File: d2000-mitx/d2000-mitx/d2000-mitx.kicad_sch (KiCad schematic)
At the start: 47 parts, among them J1 USB 3.1 + PD INPUT, J2 87715-9306, J3 USB3_A_Stacked, J4 M.2_NVME, J5 Conn_02x10_Top_Bottom, J6 M.2_WIFI, J7 ATX-24, U1 MPQ8645PGVT-0000-Z, U10 TPS784105QWDRBRQ1, U11 TPS784105QWDRBRQ1, U12 VL805 REAR I/O, U13 RP2040, U2 MPQ8645PGVT-0000-Z, U4 FUSB302B01MPX, U6 MPQ8645PGVT-0000-Z, U7 MPQ8645PGVT-0000-Z, U8 W25Q32JVSS, U9 VL805 REAR I/O, Y1 Crystal_GND23, Y2 Crystal_GND23, Y3 12MHz

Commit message: d2000-mitx: add d2000 footprint
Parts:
- U3: footprint (none) -> D2000:D2000_DDR4_BGA1144P100_3500X350
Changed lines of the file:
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@@
 			)
 		)
-		(property "Footprint" ""
+		(property "Footprint" "D2000:D2000_DDR4_BGA1144P100_3500X350"
 			(at 473.7101 161.2899 0)
 			(effects
@@
 			)
 		)
-		(property "Footprint" ""
+		(property "Footprint" "D2000:D2000_DDR4_BGA1144P100_3500X350"
 			(at 500.3801 -50.8001 0)
 			(effects
@@
 			)
 		)
-		(property "Footprint" ""
+		(property "Footprint" "D2000:D2000_DDR4_BGA1144P100_3500X350"
 			(at 297.1801 -78.7401 0)
 			(effects
@@
 			)
 		)
-		(property "Footprint" ""
+		(property "Footprint" "D2000:D2000_DDR4_BGA1144P100_3500X350"
 			(at 481.3301 386.0799 0)
 			(effects
@@
 	)
 	(symbol
-		(lib_name "D2000:D2000-E8")
 		(lib_id "D2000:D2000-E8")
 		(at 768.35 368.3 0)
@@
 			)
 		)
-		(property "Footprint" ""
+		(property "Footprint" "D2000:D2000_DDR4_BGA1144P100_3500X350"
 			(at 834.3901 116.8399 0)
 			(effects
@@
 			)
 		)
-		(property "Footprint" ""
+		(property "Footprint" "D2000:D2000_DDR4_BGA1144P100_3500X350"
 			(at 217.1701 344.1699 0)
 			(effects

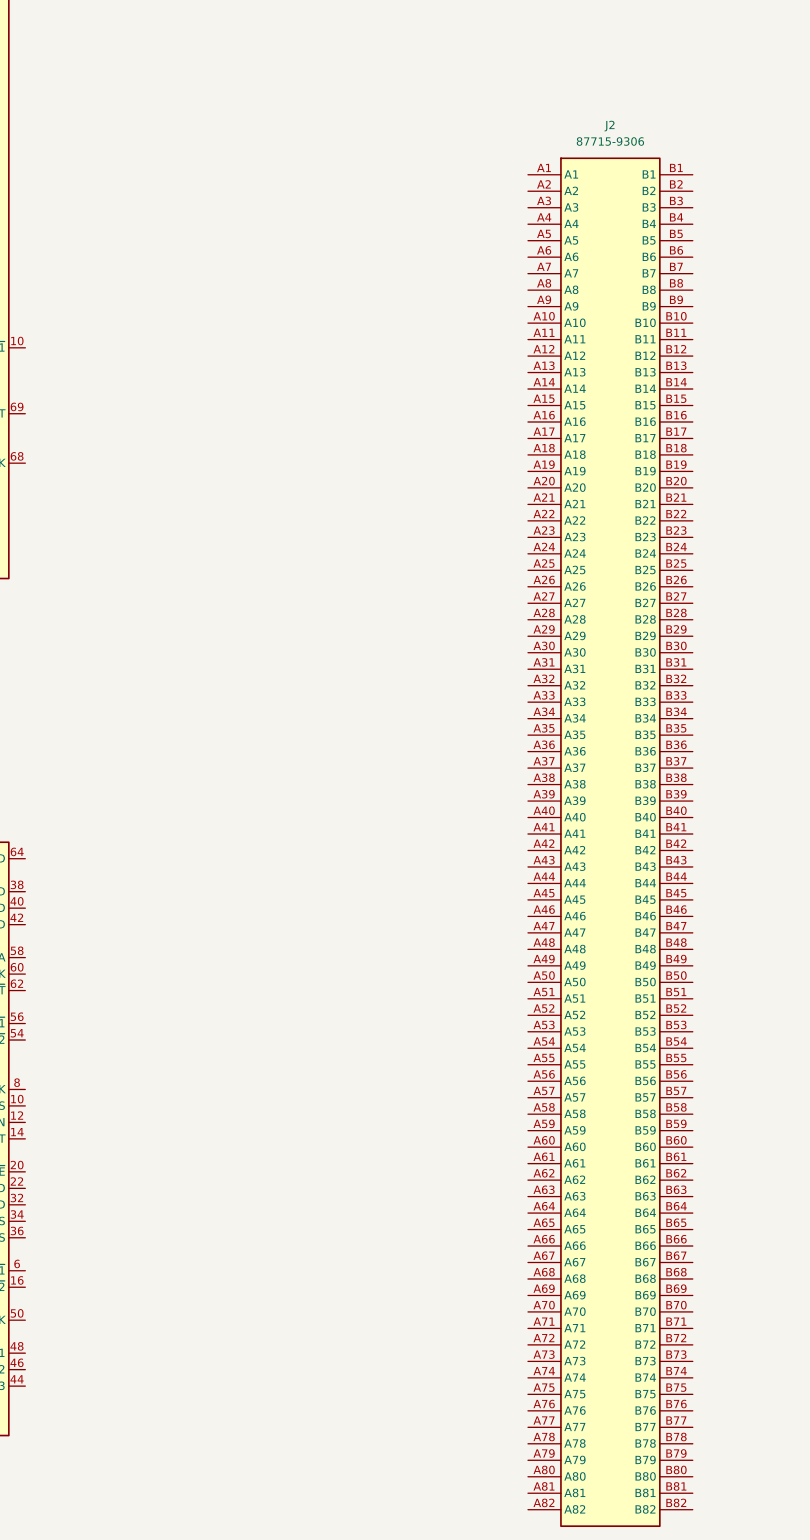
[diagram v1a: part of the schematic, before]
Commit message: d2000-mitx: slight schem tweaks, rough board placements
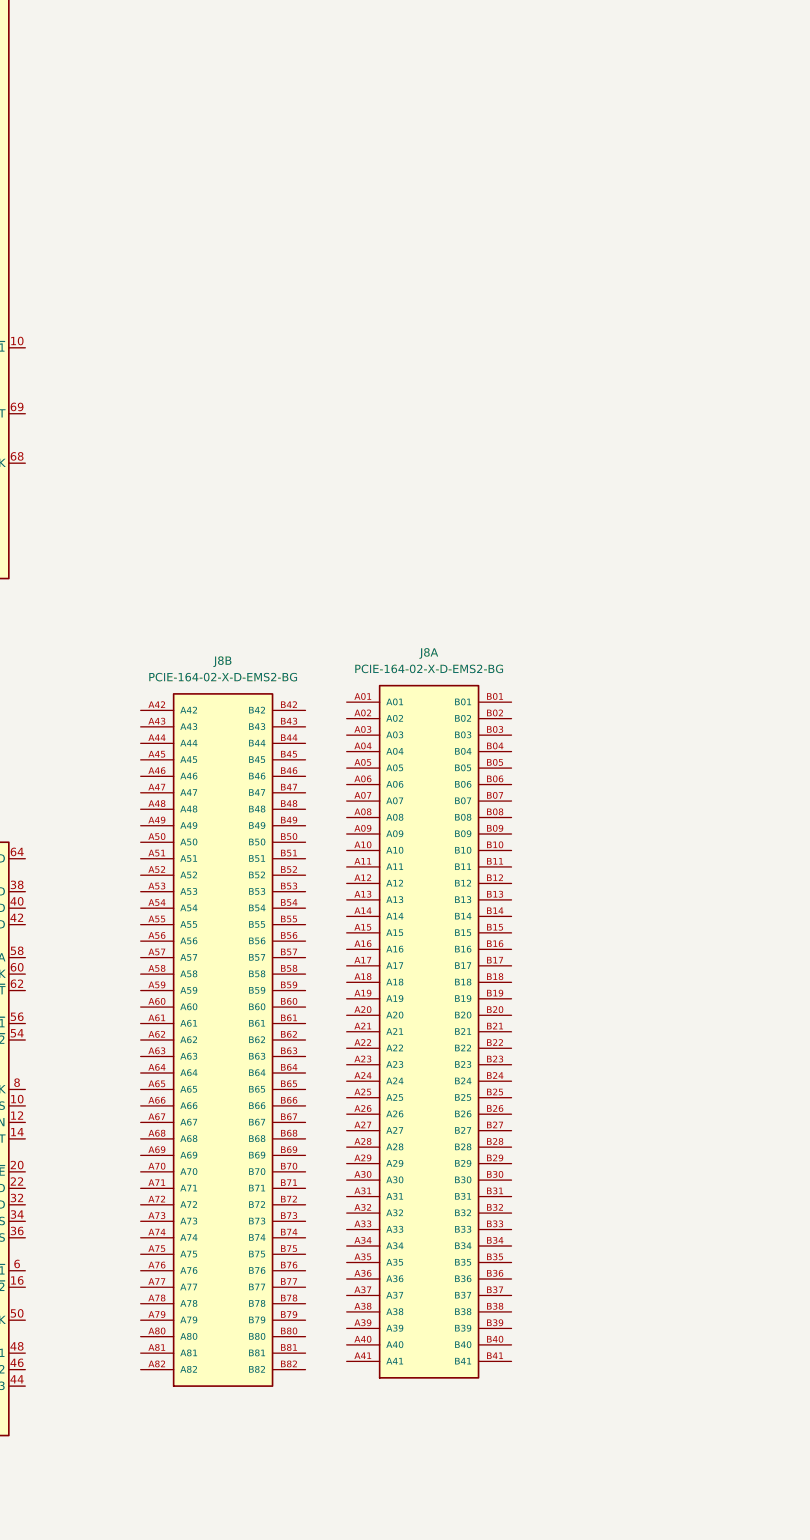
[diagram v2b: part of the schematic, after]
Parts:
- removed J2: 87715-9306, 877159306, symbol PCIe 16x MOLEX:87715-9306
- added J8: PCIE-164-02-X-D-EMS2-BG, PCIE_164_02_S_D_EMS2_BG:SAMTEC_PCIE-164-02-X-D-EMS2-BG, symbol PCIE-164-02-X-D-EMS2-BG:PCIE-164-02-X-D-EMS2-BG
- J1: footprint (none) -> Connector_USB:USB_C_Receptacle_Amphenol_12401548E4-2A
- J3: footprint (none) -> Connector_USB:USB_A_CUI_UJ2-ADH-TH_Horizontal_Stacked
- J4, J6: footprint (none) -> 2199119-3-M.2:CONN75_2199119-3_TEC
- U12, U9: footprint (none) -> Package_DFN_QFN:QFN-68-1EP_8x8mm_P0.4mm_EP5.2x5.2mm

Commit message: added major components + updated schematic + found reference schematics to steal from
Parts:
- removed C1, C2, C7, C8: 100n, Capacitor_SMD:C_0402_1005Metric, symbol Device:C
- removed C10, C3, C4, C9: 10uF, Capacitor_SMD:C_0402_1005Metric, symbol Device:C
- removed C11, C12, C5, C6: 22pF, Capacitor_SMD:C_0603_1608Metric, symbol Device:C
- removed J1: USB 3.1 + PD INPUT, Connector_USB:USB_C_Receptacle_Amphenol_12401548E4-2A, symbol Connector:USB_C_Receptacle
- removed J3: USB3_A_Stacked, Connector_USB:USB_A_CUI_UJ2-ADH-TH_Horizontal_Stacked, symbol Connector:USB3_A_Stacked
- removed J4: M.2_NVME, 2199119-3-M.2:CONN75_2199119-3_TEC, symbol Connector:Bus_M.2_Socket_M
- removed J5: Conn_02x10_Top_Bottom, symbol Connector_Generic:Conn_02x10_Top_Bottom
- removed J6: M.2_WIFI, 2199119-3-M.2:CONN75_2199119-3_TEC, symbol Connector:Bus_M.2_Socket_E
- removed J8: PCIE-164-02-X-D-EMS2-BG, PCIE_164_02_S_D_EMS2_BG:SAMTEC_PCIE-164-02-X-D-EMS2-BG, symbol PCIE-164-02-X-D-EMS2-BG:PCIE-164-02-X-D-EMS2-BG
- removed R1, R3: 6.04k, Resistor_SMD:R_0603_1608Metric, symbol Device:R_Small
- removed R2, R4: 15k, Resistor_SMD:R_0603_1608Metric, symbol Device:R_Small
- removed U10, U11: TPS784105QWDRBRQ1, Package_SON:SON-8-1EP_3x2mm_P0.5mm_EP1.4x1.6mm, symbol TPS784105QWDRBRQ1:TPS784105QWDRBRQ1
- removed U12, U9: VL805 REAR I/O, Package_DFN_QFN:QFN-68-1EP_8x8mm_P0.4mm_EP5.2x5.2mm, symbol VL805:VL805
- removed U3: ~, D2000:D2000_DDR4_BGA1144P100_3500X350, symbol D2000:D2000-E8
- removed Y1, Y2: Crystal_GND23, Crystal:Crystal_SMD_3225-4Pin_3.2x2.5mm, symbol Device:Crystal_GND23
- added H1, H2, H3, H4, H5, H6: MountingHole, MountingHole:MountingHole_3.2mm_M3_Pad, symbol Mechanical:MountingHole
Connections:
- no-connect marks 3 -> 2
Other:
- added sheet ATX PWR (15_atx_pwr.kicad_sch)
- added sheet Audio (11_audio.kicad_sch)
- added sheet Block Diagram (01_block.kicad_sch)
- added sheet CLK Block (02_clk_block.kicad_sch)
- added sheet CPLD (10_CPLD.kicad_sch)
- added sheet D2000 (03_D2000.kicad_sch)
- added sheet D2000_DIMM1 (07_D2000_DIMM1.kicad_sch)
- added sheet D2000_DIMM2 (08_D2000_DIMM2.kicad_sch)
- added sheet D2000_ETH-GPIO (05_D2000_eth_gpio.kicad_sch)
- added sheet D2000_PCIe (04_D2000_PCIe.kicad_sch)
- added sheet D2000_Power (06_D2000_power.kicad_sch)
- added sheet Headers (14_headers.kicad_sch)
- added sheet Overview (00_Cover.kicad_sch)
- added sheet PCIe (09_pcie.kicad_sch)
- added sheet Power (other) (19_power.kicad_sch)
- added sheet Serial (13_serial.kicad_sch)
- added sheet USB (12_USB.kicad_sch)
- added sheet VDDQ (17_vddq.kicad_sch)
- added sheet VDD_CORE (16_vdd_core.kicad_sch)
- added sheet VDD_IO (18_vdd_io.kicad_sch)
- title: (none) -> Bugboard-1 D2000 mITX
- moved on the sheet: J7

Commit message: update schem + pcb layout
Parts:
- removed C13, C14: 22pF, Capacitor_SMD:C_0603_1608Metric, symbol Device:C_Small
- removed H1, H2, H3, H4, H5, H6: MountingHole, MountingHole:MountingHole_3.2mm_M3_Pad, symbol Mechanical:MountingHole
- removed J7: ATX-24, symbol Connector:ATX-24
- removed R10: R, symbol Device:R_Small
- removed R11: NC, symbol Device:R
- removed R5: 10K, Resistor_SMD:R_0402_1005Metric, symbol Device:R_Small
- removed R6, R9: 1K, Resistor_SMD:R_0402_1005Metric, symbol Device:R_Small
- removed R7, R8: 22R, Resistor_SMD:R_0402_1005Metric, symbol Device:R_Small
- removed U1, U2, U6, U7: MPQ8645PGVT-0000-Z, TQFN-25_MPQ8645P_MNP, symbol MPQ8645PGVT-0000-Z:MPQ8645PGVT-0000-Z
- removed U13: RP2040, Package_DFN_QFN:QFN-56-1EP_7x7mm_P0.4mm_EP3.2x3.2mm, symbol MCU_RaspberryPi:RP2040
- removed U4: FUSB302B01MPX, Package_DFN_QFN:WQFN-14-1EP_2.5x2.5mm_P0.5mm_EP1.45x1.45mm, symbol Interface_USB:FUSB302B01MPX
- removed U8: W25Q32JVSS, Package_DFN_QFN:DFN-8-1EP_3x2mm_P0.5mm_EP1.3x1.5mm, symbol Memory_Flash:W25Q32JVSS
- removed Y3: 12MHz, Crystal:Crystal_SMD_3225-4Pin_3.2x2.5mm, symbol Device:Crystal_GND24
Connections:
- no-connect marks 2 -> 0
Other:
- sheet CLK Block renamed Power Block Diagram
- sheet Power Block Diagram: file 02_clk_block.kicad_sch -> 02_power_block.kicad_sch
- note added: "Bugboard-1 D2000 mITX"
- note added: "To-do: - Finish schematics!!! - Figure out requirements for replacing CPLD - DDR4 routing!!! - Finalize rear I/O - Finalize USB controller choice"

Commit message: d2000-mitx
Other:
- note added: "To-do: - Finish schematics!!! - Figure out requirements for replacing CPLD - M.2 board layout - MCU requirements + options - routing!!! - JLC3130 stackup - PCIe - M.2 NVMe #1 - M.2 NVMe #2 - PCIe 3.0 16x - VL805 1 & 2 - USB 3.0 - Front - Rear - Internal - Memory - DQ - DQS - Finalize rear I/O - Check against mITX docs - Check rear spacing (3d print) - Finalize USB controller choice"
- note removed: "To-do: - Finish schematics!!! - Figure out requirements for replacing CPLD - DDR4 routing!!! - Finalize rear I/O - Finalize USB controller choice"
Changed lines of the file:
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@@
 		)
 	)
-	(text "To-do:\n- Finish schematics!!!\n- Figure out requirements for replacing CPLD\n- DDR4 routing!!!\n- Finalize rear I/O\n- Finalize USB controller choice\n"
-		(exclude_from_sim no)
-		(at 30.988 75.438 0)
+	(text "To-do:\n- Finish schematics!!!\n- Figure out requirements for replacing CPLD\n	- M.2 board layout\n	- MCU requirements + options\n- routing!!!\n	- JLC3130 stackup\n	- PCIe\n		- M.2 NVMe #1\n		- M.2 NVMe #2\n		- PCIe 3.0 16x\n		- VL805 1 & 2\n	- USB 3.0\n		- Front\n		- Rear\n		- Internal\n	- Memory\n		- DQ\n		- DQS\n- Finalize rear I/O\n	- Check against mITX docs\n	- Check rear spacing (3d print)\n- Finalize USB controller choice\n"
+		(exclude_from_sim no)
+		(at 17.018 113.284 0)
 		(effects
 			(font
@@
 	)
 	(sheet
-		(at 26.67 138.43)
+		(at 165.1 64.77)
 		(size 22.86 7.62)
 		(exclude_from_sim no)
@@
 		)
 		(property "Sheetname" "D2000_DIMM1"
-			(at 26.67 137.7184 0)
+			(at 165.1 64.0584 0)
 			(effects
 				(font
@@
 		)
 		(property "Sheetfile" "07_D2000_DIMM1.kicad_sch"
-			(at 26.67 146.6346 0)
+			(at 165.1 72.9746 0)
 			(effects
 				(font
@@
 	)
 	(sheet
-		(at 250.19 123.19)
+		(at 266.7 109.22)
 		(size 22.86 7.62)
 		(exclude_from_sim no)
@@
 		)
 		(property "Sheetname" "D2000_Power"
-			(at 250.19 122.4784 0)
+			(at 266.7 108.5084 0)
 			(effects
 				(font
@@
 		)
 		(property "Sheetfile" "06_D2000_power.kicad_sch"
-			(at 250.19 131.3946 0)
+			(at 266.7 117.4246 0)
 			(effects
 				(font
@@
 	)
 	(sheet
-		(at 213.36 123.19)
+		(at 229.87 109.22)
 		(size 22.86 7.62)
 		(exclude_from_sim no)
@@
 		)
 		(property "Sheetname" "D2000_ETH-GPIO"
-			(at 213.36 122.4784 0)
+			(at 229.87 108.5084 0)
 			(effects
 				(font
@@
 		)
 		(property "Sheetfile" "05_D2000_eth_gpio.kicad_sch"
-			(at 213.36 131.3946 0)
+			(at 229.87 117.4246 0)
 			(effects
 				(font
@@
 	)
 	(sheet
-		(at 134.62 123.19)
+		(at 151.13 109.22)
 		(size 22.86 7.62)
 		(exclude_from_sim no)
@@
 		)
 		(property "Sheetname" "D2000"
-			(at 134.62 122.4784 0)
+			(at 151.13 108.5084 0)
 			(effects
 				(font
@@
 		)
 		(property "Sheetfile" "03_D2000.kicad_sch"
-			(at 134.62 131.3946 0)
+			(at 151.13 117.4246 0)
 			(effects
 				(font
@@
 	)
 	(sheet
-		(at 134.62 138.43)
+		(at 151.13 124.46)
 		(size 22.86 7.62)
 		(exclude_from_sim no)
@@
 		)
 		(property "Sheetname" "CPLD"
-			(at 134.62 137.7184 0)
+			(at 151.13 123.7484 0)
 			(effects
 				(font
@@
 		)
 		(property "Sheetfile" "10_CPLD.kicad_sch"
-			(at 134.62 146.6346 0)
+			(at 151.13 132.6646 0)
 			(effects
 				(font
@@
 	)
 	(sheet
-		(at 175.26 123.19)
+		(at 191.77 109.22)
 		(size 22.86 7.62)
 		(exclude_from_sim no)
@@
 		)
 		(property "Sheetname" "D2000_PCIe"
-			(at 175.26 122.4784 0)
+			(at 191.77 108.5084 0)
 			(effects
 				(font
@@
 		)
 		(property "Sheetfile" "04_D2000_PCIe.kicad_sch"
-			(at 175.26 131.3946 0)
+			(at 191.77 117.4246 0)
 			(effects
 				(font
@@
 	)
 	(sheet
-		(at 134.62 152.4)
+		(at 151.13 138.43)
 		(size 22.86 7.62)
 		(exclude_from_sim no)
@@
 		)
 		(property "Sheetname" "VDDQ"
-			(at 134.62 151.6884 0)
+			(at 151.13 137.7184 0)
 			(effects
 				(font
@@
 		)
 		(property "Sheetfile" "17_vddq.kicad_sch"
-			(at 134.62 160.6046 0)
+			(at 151.13 146.6346 0)
 			(effects
 				(font
@@
 	)
 	(sheet
-		(at 175.26 152.4)
+		(at 191.77 138.43)
 		(size 22.86 7.62)
 		(exclude_from_sim no)
@@
 		)
 		(property "Sheetname" "VDD_IO"
-			(at 175.26 151.6884 0)
+			(at 191.77 137.7184 0)
 			(effects
 				(font
@@
 		)
 		(property "Sheetfile" "18_vdd_io.kicad_sch"
-			(at 175.26 160.6046 0)
+			(at 191.77 146.6346 0)
 			(effects
 				(font
@@
 	)
 	(sheet
-		(at 213.36 152.4)
+		(at 229.87 138.43)
 		(size 22.86 7.62)
 		(exclude_from_sim no)
@@
 		)
 		(property "Sheetname" "Power (other)"
-			(at 213.36 151.6884 0)
+			(at 229.87 137.7184 0)
 			(effects
 				(font
@@
 		)
 		(property "Sheetfile" "19_power.kicad_sch"
-			(at 213.36 160.6046 0)
+			(at 229.87 146.6346 0)
 			(effects
 				(font
@@
 	)
 	(sheet
-		(at 95.25 152.4)
+		(at 233.68 78.74)
 		(size 22.86 7.62)
 		(exclude_from_sim no)
@@
 		)
 		(property "Sheetname" "VDD_CORE"
-			(at 95.25 151.6884 0)
+			(at 233.68 78.0284 0)
 			(effects
 				(font
@@
 		)
 		(property "Sheetfile" "16_vdd_core.kicad_sch"
-			(at 95.25 160.6046 0)
+			(at 233.68 86.9446 0)
 			(effects
 				(font
@@
 	)
 	(sheet
-		(at 213.36 138.43)
+		(at 229.87 124.46)
 		(size 22.86 7.62)
 		(exclude_from_sim no)
@@
 		)
 		(property "Sheetname" "USB"
-			(at 213.36 137.7184 0)
+			(at 229.87 123.7484 0)
 			(effects
 				(font
@@
 		)
 		(property "Sheetfile" "12_USB.kicad_sch"
-			(at 213.36 146.6346 0)
+			(at 229.87 132.6646 0)
 			(effects
 				(font
@@
 	)
 	(sheet
-		(at 26.67 123.19)
+		(at 165.1 49.53)
 		(size 22.86 7.62)
 		(exclude_from_sim no)
@@
 		)
 		(property "Sheetname" "Overview"
-			(at 26.67 122.4784 0)
+			(at 165.1 48.8184 0)
 			(effects
 				(font
@@
 		)
 		(property "Sheetfile" "00_Cover.kicad_sch"
-			(at 26.67 131.3946 0)
+			(at 165.1 57.7346 0)
 			(effects
 				(font
@@
 	)
 	(sheet
-		(at 250.19 138.43)
+		(at 266.7 124.46)
 		(size 22.86 7.62)
 		(exclude_from_sim no)
@@
 		)
 		(property "Sheetname" "Serial"
-			(at 250.19 137.7184 0)
+			(at 266.7 123.7484 0)
 			(effects
 				(font
@@
 		)
 		(property "Sheetfile" "13_serial.kicad_sch"
-			(at 250.19 146.6346 0)
+			(at 266.7 132.6646 0)
 			(effects
 				(font
@@
 	)
 	(sheet
-		(at 175.26 138.43)
+		(at 191.77 124.46)
 		(size 22.86 7.62)
 		(exclude_from_sim no)
@@
 		)
 		(property "Sheetname" "Audio"
-			(at 175.26 137.7184 0)
+			(at 191.77 123.7484 0)
 			(effects
 				(font
@@
 		)
 		(property "Sheetfile" "11_audio.kicad_sch"
-			(at 175.26 146.6346 0)
+			(at 191.77 132.6646 0)
 			(effects
 				(font
@@
 	)
 	(sheet
-		(at 60.96 152.4)
+		(at 199.39 78.74)
 		(size 22.86 7.62)
 		(exclude_from_sim no)
@@
 		)
 		(property "Sheetname" "ATX PWR"
-			(at 60.96 151.6884 0)
+			(at 199.39 78.0284 0)
 			(effects
 				(font
@@
 		)
 		(property "Sheetfile" "15_atx_pwr.kicad_sch"
-			(at 60.96 160.6046 0)
+			(at 199.39 86.9446 0)
 			(effects
 				(font
@@
 	)
 	(sheet
-		(at 60.96 138.43)
+		(at 199.39 64.77)
 		(size 22.86 7.62)
 		(exclude_from_sim no)
@@
 		)
 		(property "Sheetname" "D2000_DIMM2"
-			(at 60.96 137.7184 0)
+			(at 199.39 64.0584 0)
 			(effects
 				(font
@@
 		)
 		(property "Sheetfile" "08_D2000_DIMM2.kicad_sch"
-			(at 60.96 146.6346 0)
+			(at 199.39 72.9746 0)
 			(effects
 				(font
@@
 	)
 	(sheet
-		(at 60.96 123.19)
+		(at 199.39 49.53)
 		(size 22.86 7.62)
 		(exclude_from_sim no)
@@
 		)
 		(property "Sheetname" "Block Diagram"
-			(at 60.96 122.4784 0)
+			(at 199.39 48.8184 0)
 			(effects
 				(font
@@
 		)
 		(property "Sheetfile" "01_block.kicad_sch"
-			(at 60.96 131.3946 0)
+			(at 199.39 57.7346 0)
 			(effects
 				(font
@@
 	)
 	(sheet
-		(at 95.25 138.43)
+		(at 233.68 64.77)
 		(size 22.86 7.62)
 		(exclude_from_sim no)
@@
 		)
 		(property "Sheetname" "PCIe"
-			(at 95.25 137.7184 0)
+			(at 233.68 64.0584 0)
 			(effects
 				(font
@@
 		)
 		(property "Sheetfile" "09_pcie.kicad_sch"
-			(at 95.25 146.6346 0)
+			(at 233.68 72.9746 0)
 			(effects
 				(font
@@
 	)
 	(sheet
-		(at 95.25 123.19)
+		(at 233.68 49.53)
 		(size 22.86 7.62)
 		(exclude_from_sim no)
@@
 		)
 		(property "Sheetname" "Power Block Diagram"
-			(at 95.25 122.4784 0)
+			(at 233.68 48.8184 0)
 			(effects
 				(font
@@
 		)
 		(property "Sheetfile" "02_power_block.kicad_sch"
-			(at 95.25 131.3946 0)
+			(at 233.68 57.7346 0)
 			(effects
 				(font
@@
 	)
 	(sheet
-		(at 26.67 152.4)
+		(at 165.1 78.74)
 		(size 22.86 7.62)
 		(exclude_from_sim no)
@@
 		)
 		(property "Sheetname" "Headers"
-			(at 26.67 151.6884 0)
+			(at 165.1 78.0284 0)
 			(effects
 				(font
@@
 		)
 		(property "Sheetfile" "14_headers.kicad_sch"
-			(at 26.67 160.6046 0)
-			(effects
-				(font
+			(at 165.1 86.9446 0)
+			(effects
+				(font
